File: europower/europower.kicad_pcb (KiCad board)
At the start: 2 copper layers, 37.8 x 23.9 mm, 8 parts, among them J1 EuroPower, J2 Interconnect, U1 L7805

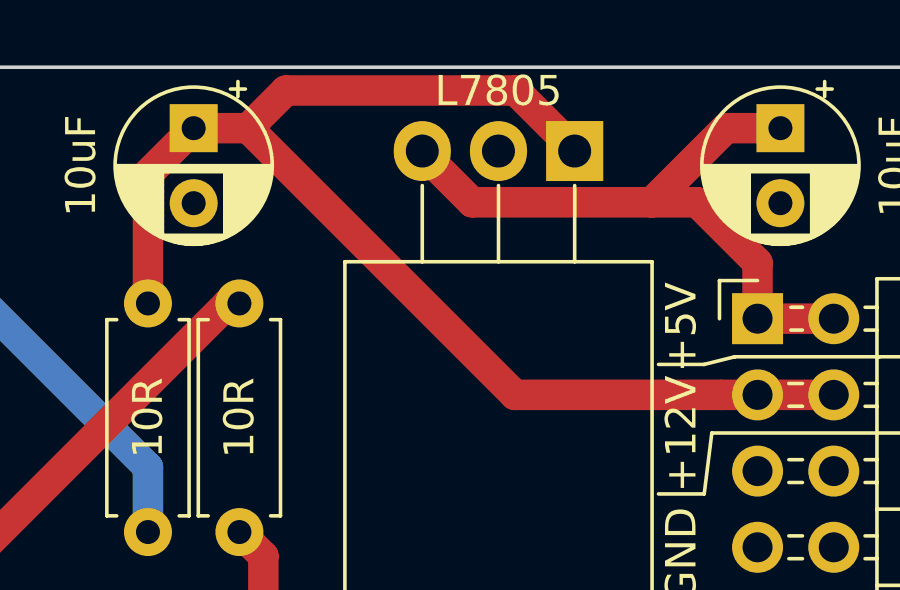
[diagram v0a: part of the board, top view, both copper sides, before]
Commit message: Extra 7805 footprint, new standard, and some order to the VCO chaos
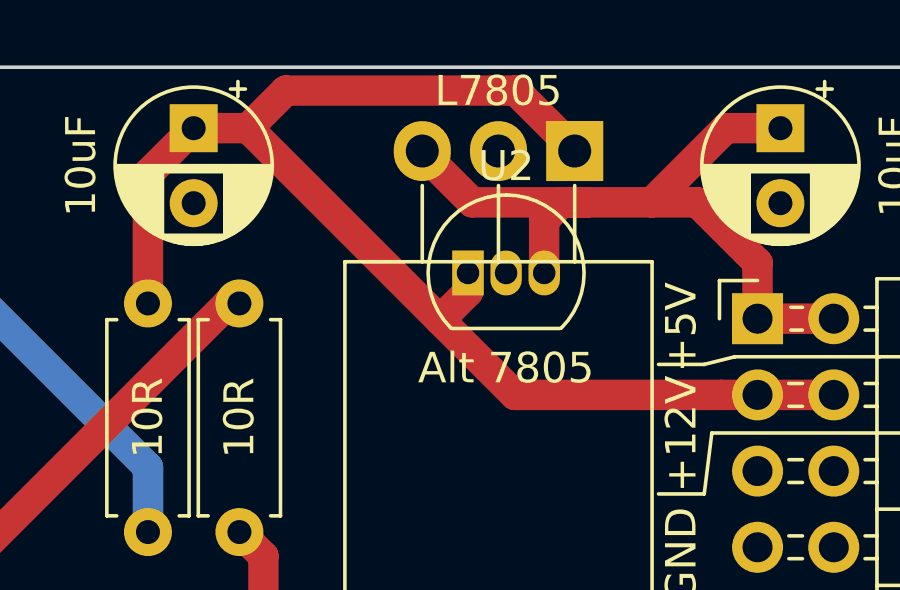
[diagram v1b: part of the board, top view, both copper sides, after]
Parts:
- added U2: L7805, Package_TO_SOT_THT:TO-92_Inline, F.Cu at (116.8, 87.6)
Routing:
- net +5V: track 22.5 -> 25.9 mm
- net +12V: track 43.8 -> 45.7 mm
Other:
- board text added: "10R may be Ferrite Beads or even shorted"
- board text added: "Alt 7805"
- board text added: "Power Filter Johan Egneblad 2020-01-11"
- board text removed: "Power Filter Johan Egneblad 2020-01-06 (Resistors may be Ferrite Beads)"
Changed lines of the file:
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@@
   (general
     (thickness 1.6)
-    (drawings 20)
-    (tracks 35)
+    (drawings 22)
+    (tracks 42)
     (zones 0)
-    (modules 8)
-    (nets 7)
+    (modules 9)
+    (nets 8)
   )
   (page A4)
@@
   )
   (setup
-    (last_trace_width 1.016)
+    (last_trace_width 0.25)
     (user_trace_width 1.016)
     (trace_clearance 0.2)
@@
   (net 5 /-12V_RAW)
   (net 6 /+12V_RAW)
+  (net 7 "Net-(U2-Pad2)")
   (net_class Default "This is the default net class."
     (clearance 0.2)
@@
     (add_net /-12V_RAW)
     (add_net GND)
+    (add_net "Net-(U2-Pad2)")
+  )
+  (module Package_TO_SOT_THT:TO-92_Inline (layer F.Cu)
+    (at 116.84 87.63)
+    (descr "TO-92 leads in-line, narrow, oval pads, drill 0.75mm (see NXP sot054_po.pdf)")
+    (tags "to-92 sc-43 sc-43a sot54 PA33 transistor")
+    (fp_text reference U2 (at 1.27 -3.56) (layer F.SilkS)
+      (effects (font (size 1 1) (thickness 0.15)))
+    )
+    (fp_text value L7805 (at 1.27 2.79) (layer F.Fab)
+      (effects (font (size 1 1) (thickness 0.15)))
+    )
+    (fp_arc (start 1.27 0) (end 1.27 -2.6) (angle 135) (layer F.SilkS) (width 0.12))
+    (fp_arc (start 1.27 0) (end 1.27 -2.48) (angle -135) (layer F.Fab) (width 0.1))
+    (fp_arc (start 1.27 0) (end 1.27 -2.6) (angle -135) (layer F.SilkS) (width 0.12))
+    (fp_arc (start 1.27 0) (end 1.27 -2.48) (angle 135) (layer F.Fab) (width 0.1))
+    (fp_line (start 4 2.01) (end -1.46 2.01) (layer F.CrtYd) (width 0.05))
+    (fp_line (start 4 2.01) (end 4 -2.73) (layer F.CrtYd) (width 0.05))
+    (fp_line (start -1.46 -2.73) (end -1.46 2.01) (layer F.CrtYd) (width 0.05))
+    (fp_line (start -1.46 -2.73) (end 4 -2.73) (layer F.CrtYd) (width 0.05))
+    (fp_line (start -0.5 1.75) (end 3 1.75) (layer F.Fab) (width 0.1))
+    (fp_line (start -0.53 1.85) (end 3.07 1.85) (layer F.SilkS) (width 0.12))
+    (fp_text user %R (at 1.27 -3.56) (layer F.Fab)
+      (effects (font (size 1 1) (thickness 0.15)))
+    )
+    (pad 1 thru_hole rect (at 0 0) (size 1.05 1.5) (drill 0.75) (layers *.Cu *.Mask)
+      (net 2 +12V))
+    (pad 3 thru_hole oval (at 2.54 0) (size 1.05 1.5) (drill 0.75) (layers *.Cu *.Mask)
+      (net 4 +5V))
+    (pad 2 thru_hole oval (at 1.27 0) (size 1.05 1.5) (drill 0.75) (layers *.Cu *.Mask)
+      (net 7 "Net-(U2-Pad2)"))
+    (model ${KISYS3DMOD}/Package_TO_SOT_THT.3dshapes/TO-92_Inline.wrl
+      (at (xyz 0 0 0))
+      (scale (xyz 1 1 1))
+      (rotate (xyz 0 0 0))
+    )
   )
   (module Package_TO_SOT_THT:TO-220-3_Horizontal_TabDown (layer F.Cu)
@@
     )
   )
-  (gr_text "Power Filter\nJohan Egneblad\n2020-01-06\n(Resistors may be\nFerrite Beads)" (at 117.348 91.948) (layer B.SilkS)
+  (gr_text "10R may be \nFerrite Beads\nor even shorted" (at 106.045 101.6) (layer B.SilkS)
+    (effects (font (size 0.7 0.7) (thickness 0.1)) (justify left mirror))
+  )
+  (gr_text "Alt 7805" (at 118.11 90.805) (layer F.SilkS)
+    (effects (font (size 1.016 1.016) (thickness 0.1016)))
+  )
+  (gr_text "Power Filter\nJohan Egneblad\n2020-01-11" (at 117.475 93.345) (layer B.SilkS)
     (effects (font (size 1 1) (thickness 0.15)) (justify mirror))
   )
@@
   (segment (start 125.289919 91.694) (end 126.492 91.694) (width 1.016) (layer F.Cu) (net 2))
   (segment (start 118.402 91.694) (end 125.289919 91.694) (width 1.016) (layer F.Cu) (net 2))
-  (segment (start 109.512 82.804) (end 118.402 91.694) (width 1.016) (layer F.Cu) (net 2))
   (segment (start 107.696 82.804) (end 109.512 82.804) (width 1.016) (layer F.Cu) (net 2))
   (segment (start 126.492 91.694) (end 129.032 91.694) (width 1.016) (layer F.Cu) (net 2))
+  (segment (start 116.84 88.265) (end 115.9065 89.1985) (width 1.016) (layer F.Cu) (net 2))
+  (segment (start 116.84 87.63) (end 116.84 88.265) (width 1.016) (layer F.Cu) (net 2))
+  (segment (start 109.512 82.804) (end 115.9065 89.1985) (width 1.016) (layer F.Cu) (net 2))
+  (segment (start 115.9065 89.1985) (end 118.402 91.694) (width 1.016) (layer F.Cu) (net 2))
   (segment (start 108.82737 102.322) (end 107.696 102.322) (width 1.016) (layer F.Cu) (net 3))
   (segment (start 110.019999 97.065999) (end 110.019999 101.129371) (width 1.016) (layer F.Cu) (net 3))
@@
   (segment (start 125.438 82.804) (end 127.254 82.804) (width 1.016) (layer F.Cu) (net 4))
   (segment (start 122.967999 85.274001) (end 125.438 82.804) (width 1.016) (layer F.Cu) (net 4))
-  (segment (start 116.976501 85.274001) (end 122.967999 85.274001) (width 1.016) (layer F.Cu) (net 4))
   (segment (start 115.316 83.6135) (end 116.976501 85.274001) (width 1.016) (layer F.Cu) (net 4))
   (segment (start 115.316 83.566) (end 115.316 83.6135) (width 1.016) (layer F.Cu) (net 4))
@@
   (segment (start 126.492 89.154) (end 126.492 87.288) (width 1.016) (layer F.Cu) (net 4))
   (segment (start 126.492 89.154) (end 129.032 89.154) (width 1.016) (layer F.Cu) (net 4))
+  (segment (start 119.38 87.63) (end 119.38 85.864) (width 1.016) (layer F.Cu) (net 4))
+  (segment (start 116.976501 85.274001) (end 120.834001 85.274001) (width 1.016) (layer F.Cu) (net 4))
+  (segment (start 119.969999 85.274001) (end 120.834001 85.274001) (width 1.016) (layer F.Cu) (net 4))
+  (segment (start 119.38 85.864) (end 119.969999 85.274001) (width 1.016) (layer F.Cu) (net 4))
+  (segment (start 120.834001 85.274001) (end 122.967999 85.274001) (width 1.016) (layer F.Cu) (net 4))
   (segment (start 97.155 97.79) (end 99.695 97.79) (width 1.016) (layer F.Cu) (net 5))
   (segment (start 108.839 88.646) (end 109.22 88.646) (width 1.016) (layer F.Cu) (net 5))
